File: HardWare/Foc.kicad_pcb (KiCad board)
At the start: 2 copper layers, 60 x 40 mm, 157 parts, among them J1 复用Typec, J2 hall, J3 Conn_01x03, J4 hall, J5 Conn_01x03, J6 SWD, J7 inp, J8 XH2.54, J9 SPI_conn, Q1 Q_NMOS_SGD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

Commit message: Add Rules
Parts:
- C19: moved to B.Cu
- J6: footprint Connector_PinSocket_2.54mm:PinSocket_1x05_P2.54mm_Horizontal -> Connector_PinSocket_2.54mm:PinSocket_1x05_P2.54mm_Vertical
- TP1: footprint TestPoint:TestPoint_THTPad_D2.0mm_Drill1.0mm -> TestPoint:TestPoint_Pad_1.0x1.0mm
- moved C19 83.4 mm to (142.0, 148.0), turned to 90 degrees
- moved C7 78.6 mm to (163.2, 75.8)
- moved J2 62.8 mm to (152.2, 158.0)
- moved C51 22.3 mm to (83.0, 138.5)
- moved J4 11.4 mm to (73.2, 181.8)
- moved D2 7.28 mm to (136.0, 151.2)
- moved L1 6.43 mm to (135.1, 145.8)
- moved J3 3.26 mm to (74.0, 172.5)
- moved J5 1.50 mm to (99.5, 172.5)
- moved Q1 1.47 mm to (81.8, 165.0)
- moved Q2 1.47 mm to (73.5, 164.8)
- moved Q3 1.47 mm to (81.7, 157.8)
- moved Q4 1.47 mm to (65.0, 164.8)
- moved Q5 1.47 mm to (73.4, 157.8)
- moved Q6 1.47 mm to (65.0, 157.8)
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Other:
- copper layers 2 -> 4

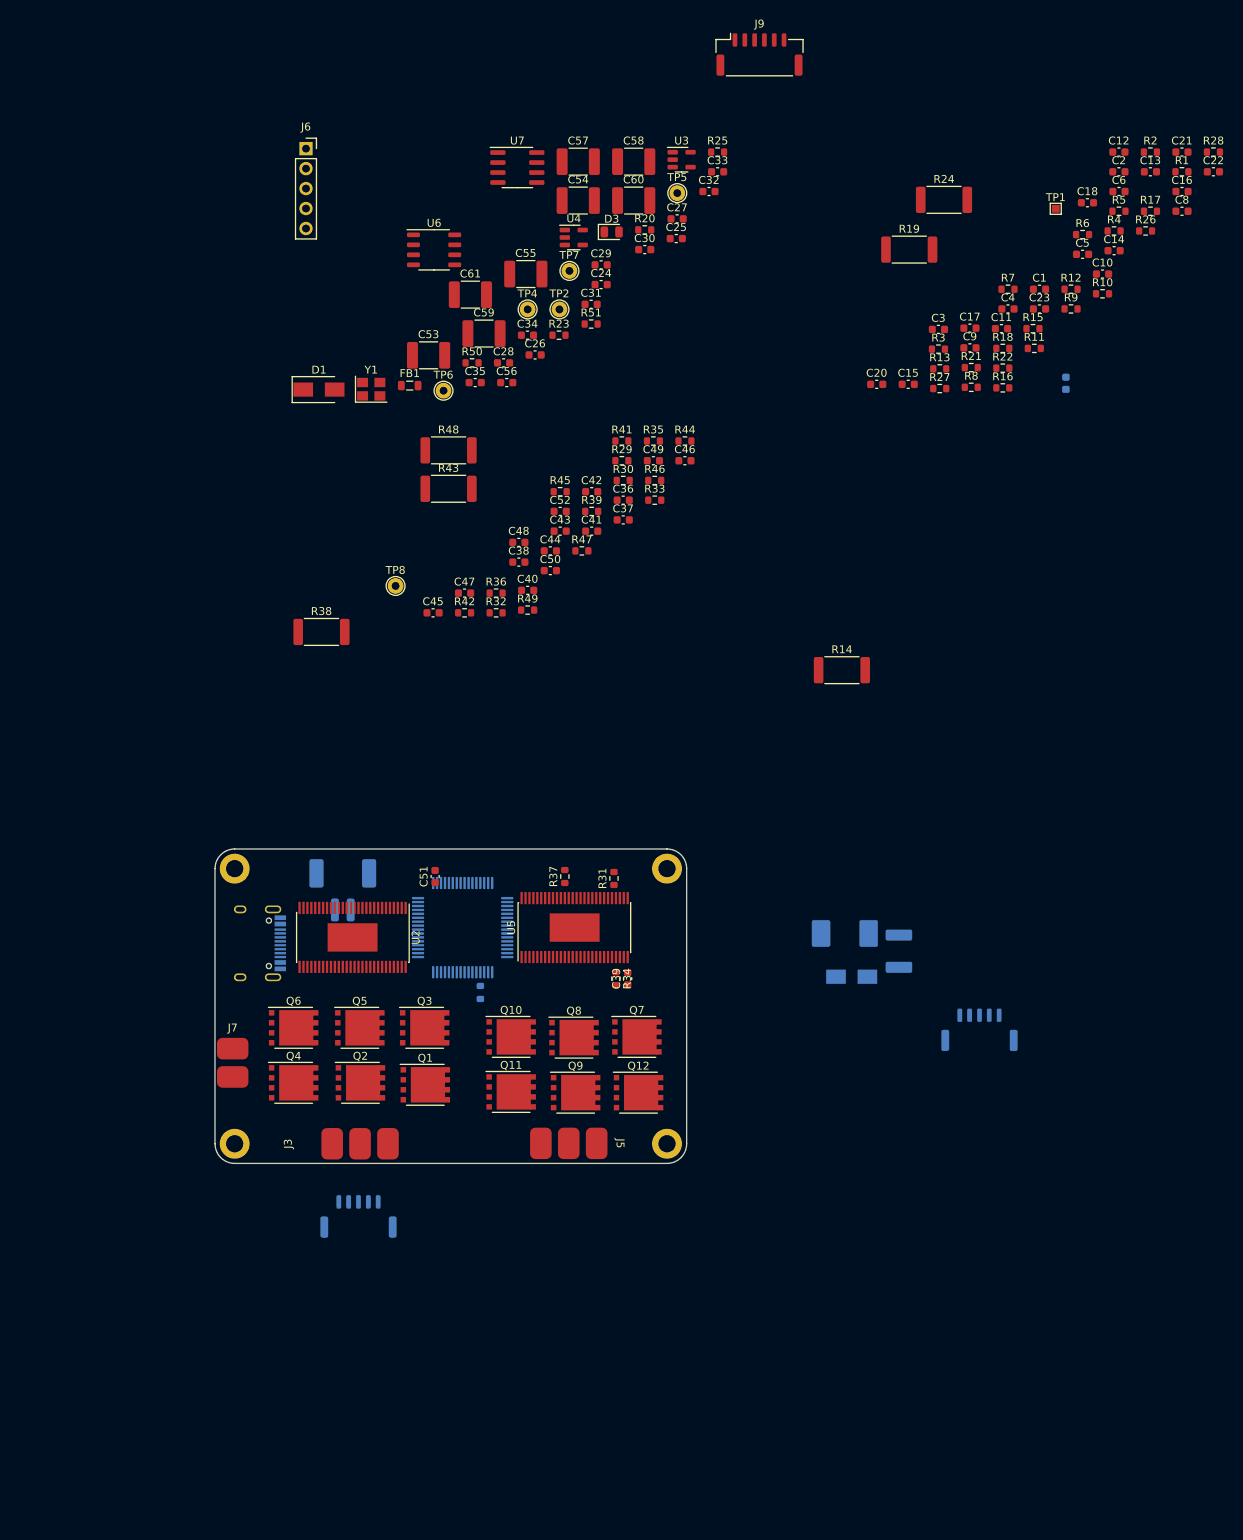
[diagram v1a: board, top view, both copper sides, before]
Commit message: 增加一些功率器件有关的pcb电路
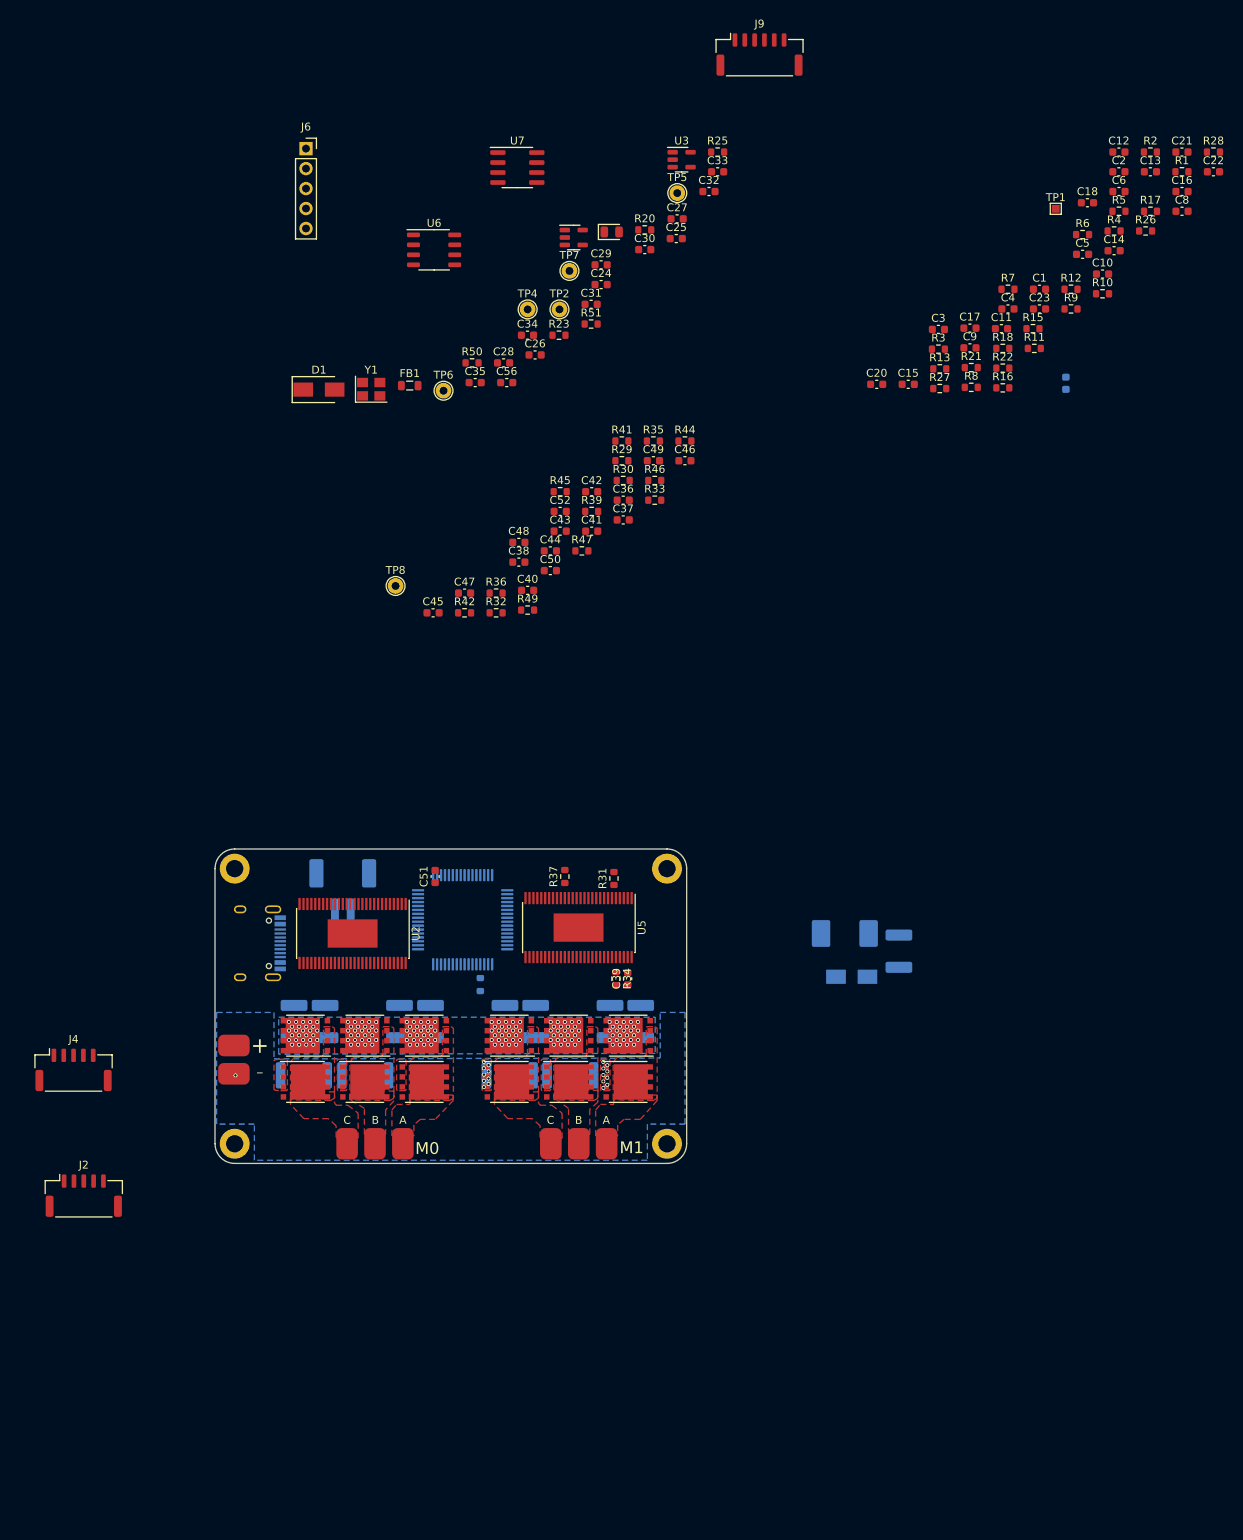
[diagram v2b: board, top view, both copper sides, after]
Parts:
- removed R14, R38: 0.0005, Resistor_SMD:R_2512_6332Metric
- C53, C54, C55, C57, C58, C59, C60, C61, R19, R24, R48: moved to B.Cu
- J2, J4: moved to F.Cu
- R43: value 0.0005 -> locked; moved to B.Cu
- moved R24 138.0 mm to (66.3, 163.8)
- moved R19 125.8 mm to (74.1, 163.8)
- moved J2 115.9 mm to (38.3, 179.1), turned to 0 degrees
- moved C57 114.0 mm to (69.0, 156.9), turned to 90 degrees
- moved C58 112.4 mm to (82.4, 156.9), turned to 90 degrees
- moved C54 110.5 mm to (65.0, 156.9), turned to 90 degrees
- moved C60 108.6 mm to (78.5, 156.9), turned to 90 degrees
- moved C55 95.1 mm to (95.8, 156.9), turned to 90 degrees
- moved C61 95.0 mm to (109.2, 156.9), turned to 90 degrees
- moved C59 89.0 mm to (105.2, 156.9), turned to 90 degrees
- moved C53 85.3 mm to (91.9, 156.9), turned to 90 degrees
- moved R48 79.9 mm to (92.5, 163.8)
- moved R43 76.2 mm to (100.2, 163.8)
- moved J4 40.8 mm to (37.0, 163.1), turned to 0 degrees
- moved Q12 16.5 mm to (92.4, 164.6)
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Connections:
- net Net-(J3-Pad1) renamed /controller/A
- net Net-(J3-Pad2) renamed /controller/B
- net Net-(J3-Pad3) renamed /controller/C
- net Net-(J5-Pad1) renamed /motor2/A
- net Net-(J5-Pad2) renamed /motor2/B
- net Net-(J5-Pad3) renamed /motor2/C
- Q2 pad 1: /controller/M1_SL_A -> GND1
- Q8 pad 1: /motor2/M2_SL_A -> GND1
- U2 pad 44: /controller/M1_SL_A -> GND1
- U5 pad 44: /motor2/M2_SL_A -> GND1
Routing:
- net VDC: vias 0 -> 162
- net GND1: vias 0 -> 10
- net /motor2/M2_SL_C: vias 0 -> 9
- added copper zone on F.Cu, net /controller/A
- added copper zone on F.Cu, net /controller/B
- added copper zone on F.Cu, net /controller/C
- added copper zone on F.Cu, net /controller/M1_SL_B
- added copper zone on F.Cu, net /controller/M1_SL_C
- added copper zone on F.Cu, net /motor2/A
- added copper zone on F.Cu, net /motor2/B
- added copper zone on F.Cu, net /motor2/C
- added copper zone on F.Cu, net /motor2/M2_SL_B
- added copper zone on F.Cu, net /motor2/M2_SL_C
- added copper zone on B.Cu, net GND1
- added copper zone on F.Cu, net GND1
- added copper zone on B.Cu, net VDC
- added copper zone on In1.Cu, net VDC
- added copper zone on In2.Cu, net VDC
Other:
- board text added: "+"
- board text added: "-"
- board text added: "A"
- board text added: "B"
- board text added: "C"
- board text added: "M0"
- board text added: "M1"

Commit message: 修改硬件电路
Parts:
- D1: moved to B.Cu
- R40: moved to F.Cu
- moved R40 84.5 mm to (114.7, 71.8), turned to 180 degrees
- moved D1 70.3 mm to (67.1, 146.8), turned to -90 degrees
- moved R30 64.8 mm to (94.1, 151.6), turned to -90 degrees
- moved R46 64.4 mm to (100.1, 151.6), turned to -90 degrees
- moved C19 64.1 mm to (78.2, 141.9), turned to 180 degrees
- moved R33 62.2 mm to (98.6, 151.6), turned to -90 degrees
- moved C36 62.0 mm to (95.6, 151.6), turned to -90 degrees
- moved U1 61.5 mm to (146.2, 129.2)
- moved L1 58.1 mm to (77.1, 148.4), turned to 90 degrees
- moved D2 53.6 mm to (82.5, 148.8), turned to -90 degrees
- moved C39 18.3 mm to (94.2, 138.9), turned to -90 degrees
- moved R31 15.5 mm to (97.1, 151.6), turned to -90 degrees
- moved J8 15.2 mm to (74.2, 125.3)
- moved U2 2.14 mm to (74.5, 145.0)
- moved U5 0.60 mm to (100.7, 145.3)
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- renumbered R19 to Re
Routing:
- net VDC: vias 162 -> 185
- net GND1: vias 10 -> 47
- net /motor2/M2_SL_C: vias 9 -> 12
- net /motor2/M2_SL_B: vias 0 -> 12
- net /controller/M1_SL_C: vias 0 -> 12
- net /controller/M1_SL_B: vias 0 -> 12
- added copper zone on B.Cu, net /controller/M1_SL_B
- added copper zone on B.Cu, net /controller/M1_SL_C
- added copper zone on B.Cu, net /motor2/M2_SL_B
- added copper zone on B.Cu, net /motor2/M2_SL_C

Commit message: 修改一些BUG
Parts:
- removed TP1: GVDD1, TestPoint:TestPoint_Pad_1.0x1.0mm
- removed TP2, TP4, TP5, TP6, TP7: TP, TestPoint:TestPoint_THTPad_D2.0mm_Drill1.0mm
- removed TP8: GVDD1, TestPoint:TestPoint_THTPad_D2.0mm_Drill1.0mm
- C19, C53, C54, C55, C57, C59, C60, C61: value 47uf -> 10uf; footprint Capacitor_SMD:C_1812_4532Metric -> Capacitor_SMD:C_1210_3225Metric
- C58: value 47uf -> locked; footprint Capacitor_SMD:C_1812_4532Metric -> Capacitor_SMD:C_1210_3225Metric
- C7: moved to F.Cu
- J2, J4: footprint Connector_Molex:Molex_CLIK-Mate_502386-0570_1x05-1MP_P1.25mm_Horizontal -> USER:M1010RS-05P; moved to B.Cu
- U3, U4, U6: moved to B.Cu
- moved C22 159.5 mm to (86.9, 176.9), turned to 90 degrees
- moved R28 157.8 mm to (93.4, 176.9), turned to 90 degrees
- moved C21 154.6 mm to (95.3, 176.9), turned to 90 degrees
- moved C2 148.9 mm to (39.2, 120.0)
- moved R12 148.9 mm to (33.1, 134.9)
- moved R17 148.9 mm to (43.2, 125.0)
- moved R5 148.9 mm to (39.2, 125.0)
- moved R6 148.9 mm to (34.6, 128.0)
- moved R15 148.9 mm to (42.4, 161.3)
- moved R26 145.7 mm to (91.6, 176.9), turned to 90 degrees
- moved C16 140.6 mm to (79.4, 151.5), turned to 90 degrees
- moved C8 140.4 mm to (65.8, 138.3), turned to -90 degrees
- moved R16 140.0 mm to (41.9, 158.5)
- moved C13 137.3 mm to (82.7, 151.4), turned to 90 degrees
- moved C20 136.4 mm to (40.0, 169.5)
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- renumbered Re to R19
